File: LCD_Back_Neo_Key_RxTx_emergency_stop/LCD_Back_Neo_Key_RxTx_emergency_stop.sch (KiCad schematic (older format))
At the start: 4 parts, among them J1 Screw_Terminal_01x14, J3 Conn_01x08_Male_KeyPad, U1 DC-DC_Stepdown-Zimprich

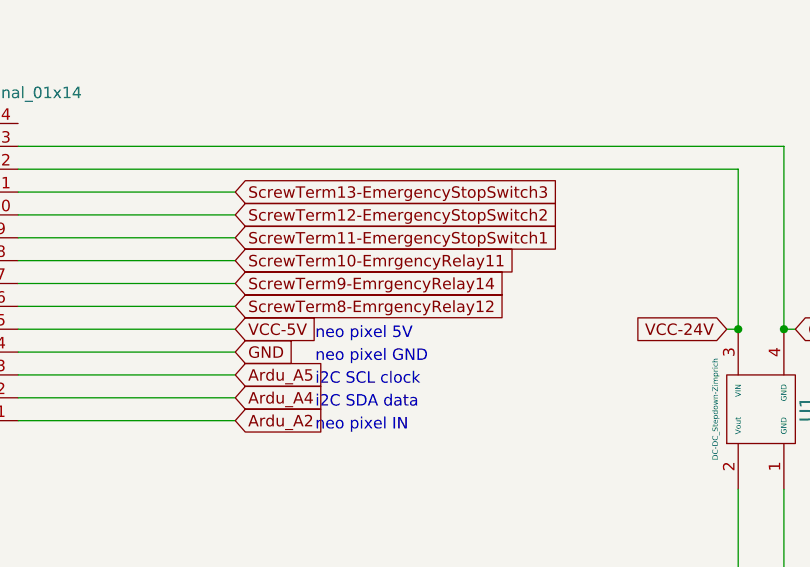
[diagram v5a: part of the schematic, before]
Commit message: contact all on PCB
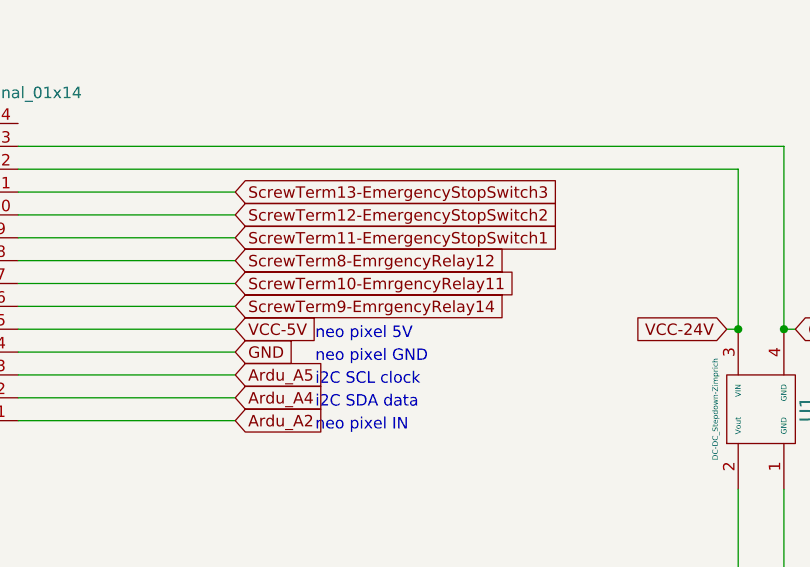
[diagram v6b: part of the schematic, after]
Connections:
- net ScrewTerm10-EmrgencyRelay11: now also J1.7 (Pin_7); no longer J1.8 (Pin_8)
- net ScrewTerm8-EmrgencyRelay12: now also J1.8 (Pin_8); no longer J1.6 (Pin_6)
- net ScrewTerm9-EmrgencyRelay14: now also J1.6 (Pin_6); no longer J1.7 (Pin_7)
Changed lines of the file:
@@
 	-1   0    0    1
 $EndComp
+Text GLabel 1950 3750 2    50   Input ~ 0
+ScrewTerm8-EmrgencyRelay12
 Text GLabel 1950 3950 2    50   Input ~ 0
-ScrewTerm8-EmrgencyRelay12
+ScrewTerm9-EmrgencyRelay14
 Text GLabel 1950 3850 2    50   Input ~ 0
-ScrewTerm9-EmrgencyRelay14
-Text GLabel 1950 3750 2    50   Input ~ 0
 ScrewTerm10-EmrgencyRelay11
 Text GLabel 1950 3650 2    50   Input ~ 0
@@
 ScrewTerm13-EmergencyStopSwitch3
 Wire Wire Line
+	1000 3750 1950 3750
+Wire Wire Line
 	1000 3950 1950 3950
 Wire Wire Line
 	1000 3850 1950 3850
 Wire Wire Line
-	1000 3750 1950 3750
-Wire Wire Line
 	1000 3650 1950 3650
